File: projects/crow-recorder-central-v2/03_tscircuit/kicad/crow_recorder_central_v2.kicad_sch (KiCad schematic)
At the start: 194 parts, among them J1 C381116, J10 C9900035627, J2 C3020560, J3 C9900035627, J4 C9900035627, J5 C9900035627, J6 C9900035627, J7 C9900035627, J8 C9900035627, J9 C9900035627, Q1 C15127, Q2 C20917, U1 C6938291, U10 C6035451, U2 C181312, U3 C181312, U4 C232798, U5 C82317, U6 C2909890, U7 C5224055, U8 C5224055, U9 C79924, Y1 C2762192

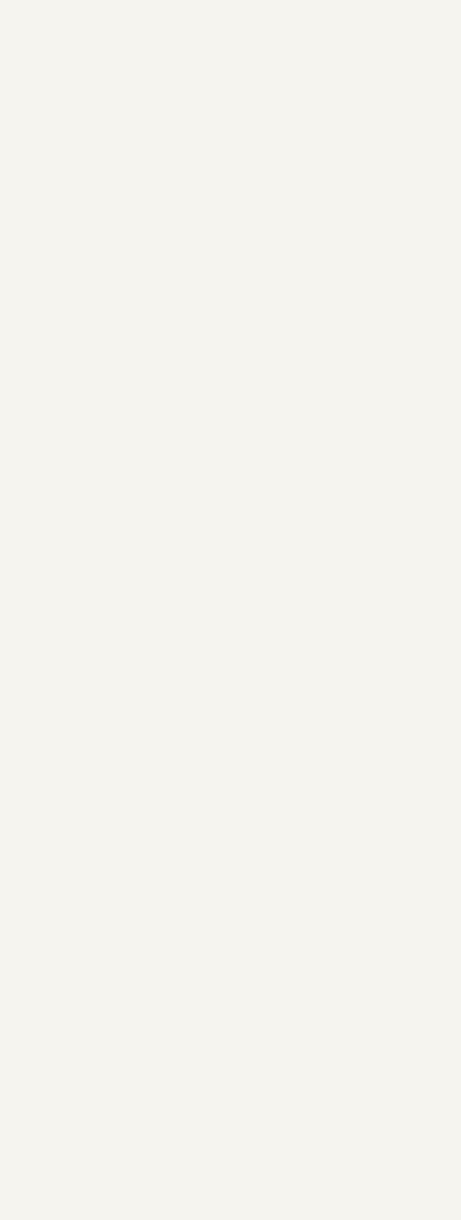
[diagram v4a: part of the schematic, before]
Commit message: crow-central v1.2: XU316 core decoupling to vendor minimum — 13x 100nF on 0V9, routing gate GREEN
Driver: 2nd external v1.1 review (EXT2-F1, archived verbatim in 08_reviews
with provenance + orchestrator verification): 8x 100nF on the 0V9 core rail
for 15 core-VDD pins vs the vendor minimum. Vendor number VERIFIED at the
source, not taken from the reviewer: XU316-1024-TQ128 ds XM-014532-PC-2.0.0
§14 'Integration' p.29 — 'Place many (at least 12) 100 nF low inductance
multi-layer ceramic capacitors close to the chip' (§H.2 p.92 agrees).

The fix (all at source, canon M3):
- tsx 8->13 C_c caps; manifest +5; promoted-sch IN-PLACE surgery (LV-strap
  precedent — regeneration drops the P5VA_4/MID2P doglegs): measured netlist
  diff vs v1.1 = EXACTLY {C_c9..C_c13} x {0V9,GND}.
- Placement: 5 anchors at scan-verified spots hard against the under-served
  pins; the 32 U1-cluster floaters PINNED at their v1.1 positions (the new
  anchors changed the legalizer walk and moved all 32 — measured — which
  would have invalidated the whole promoted chain).
- C_b0v9 slot swap: U1 courtyard vs the C_c1/C_b0v9 row leaves no 0402 slot
  at pins 50/54; the 10uF bulk (no pin-adjacency requirement, ds §14) moved
  3.75mm south; C_c11/C_c13 take its slot at 2.01/2.02mm from pins 50/54.
- Chain surgery: TDI F.Cu run -> In3 (frees the south band); 0V9 feeder
  rerouted at 0.4; 4x 0.30mm taps into pads 14/50/54/95 with scoped floors
  (0.4 into a 0.4mm-pitch row violates neighbor clearance by construction);
  C_b0v9 B.Cu feed with 2 vias; title caption relocated.
- C_c11 pad2 starved_thermal -> pad_overrides FULL (golden rule 9).

Gate: rebuild_reuse.sh from committed source = DRC 0/0/0 (severity-all +
refill + schematic-parity); port nets 115/115 + 8/8. Survival measured:
USB pair 23.621/23.511mm skew 0.110mm all-0.125 F.Cu 0 vias; U1 EP 16x
0.3/0.15 GND vias; LV straps 40/43/52 unconnected. Worst pin-to-nearest-cap
3.22mm. Per-pin map in journal/routing.md.

Co-Authored-By: Claude Opus 5 <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
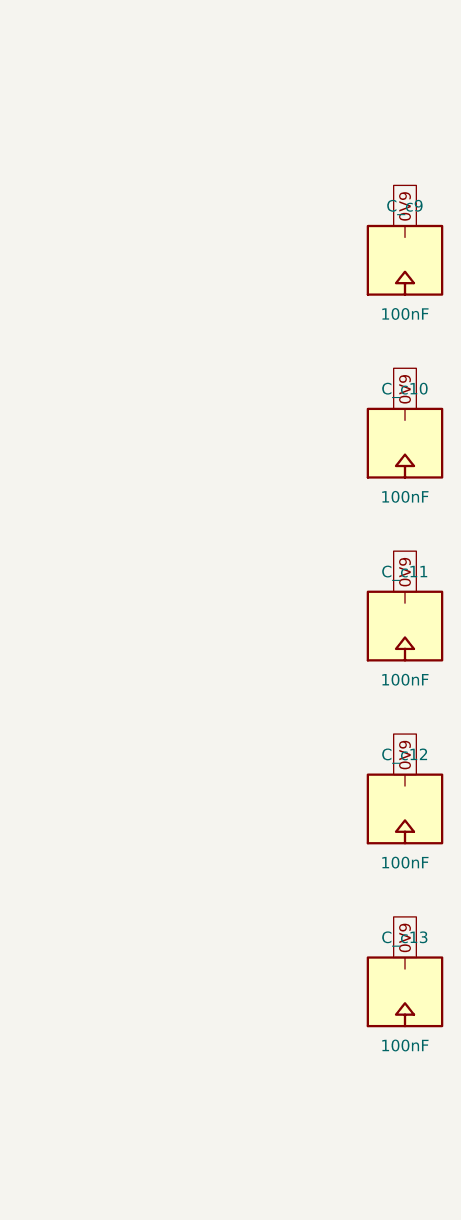
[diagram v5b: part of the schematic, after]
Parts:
- added C_c10, C_c11, C_c12, C_c13, C_c9: 100nF, Capacitor_SMD:C_0402_1005Metric, symbol elt:SYM_C_c8
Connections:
- net 0V9: now also C_c10.1, C_c11.1, C_c12.1, C_c13.1, C_c9.1
- net GND: now also C_c10.2, C_c11.2, C_c12.2, C_c13.2, C_c9.2
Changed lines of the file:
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@@
     (instances (project "crow_recorder_central_v2" (path "/735d9c2a-b8fe-44e1-a7cf-81ca2fca9464" (reference "R_inj2") (unit 1))))
+  )
+  (symbol (lib_id "elt:SYM_C_c8") (at 609.600 80.010 0) (unit 1) (in_bom yes) (on_board yes) (dnp no)
+    (property "Reference" "C_c9" (at 609.600 74.000 0) (effects (font (size 1.27 1.27))))
+    (property "Value" "100nF" (at 609.600 86.020 0) (effects (font (size 1.27 1.27))))
+    (property "Footprint" "Capacitor_SMD:C_0402_1005Metric" (at 609.600 80.010 0) (effects (font (size 1.27 1.27)) hide))
+    (pin "1")
+    (pin "2")
+    (instances (project "crow_recorder_central_v2" (path "/735d9c2a-b8fe-44e1-a7cf-81ca2fca9464" (reference "C_c9") (unit 1))))
+  )
+  (global_label "0V9" (shape passive) (at 609.600 76.200 90) (fields_autoplaced) (effects (font (size 1.27 1.27)) (justify left)))
+  (symbol (lib_id "elt:GND") (at 609.600 83.820 180) (unit 1) (in_bom no) (on_board yes) (dnp no)
+    (property "Reference" "#PWR145" (at 609.600 83.820 0) (effects (font (size 1.27 1.27)) hide))
+    (property "Value" "GND" (at 609.600 83.820 0) (effects (font (size 1.27 1.27)) hide))
+    (property "Footprint" "" (at 609.600 83.820 0) (effects (font (size 1.27 1.27)) hide))
+    (pin "1")
+    (instances (project "crow_recorder_central_v2" (path "/735d9c2a-b8fe-44e1-a7cf-81ca2fca9464" (reference "#PWR145") (unit 1))))
+  )
+  (symbol (lib_id "elt:SYM_C_c8") (at 609.600 100.330 0) (unit 1) (in_bom yes) (on_board yes) (dnp no)
+    (property "Reference" "C_c10" (at 609.600 94.320 0) (effects (font (size 1.27 1.27))))
+    (property "Value" "100nF" (at 609.600 106.340 0) (effects (font (size 1.27 1.27))))
+    (property "Footprint" "Capacitor_SMD:C_0402_1005Metric" (at 609.600 100.330 0) (effects (font (size 1.27 1.27)) hide))
+    (pin "1")
+    (pin "2")
+    (instances (project "crow_recorder_central_v2" (path "/735d9c2a-b8fe-44e1-a7cf-81ca2fca9464" (reference "C_c10") (unit 1))))
+  )
+  (global_label "0V9" (shape passive) (at 609.600 96.520 90) (fields_autoplaced) (effects (font (size 1.27 1.27)) (justify left)))
+  (symbol (lib_id "elt:GND") (at 609.600 104.140 180) (unit 1) (in_bom no) (on_board yes) (dnp no)
+    (property "Reference" "#PWR146" (at 609.600 104.140 0) (effects (font (size 1.27 1.27)) hide))
+    (property "Value" "GND" (at 609.600 104.140 0) (effects (font (size 1.27 1.27)) hide))
+    (property "Footprint" "" (at 609.600 104.140 0) (effects (font (size 1.27 1.27)) hide))
+    (pin "1")
+    (instances (project "crow_recorder_central_v2" (path "/735d9c2a-b8fe-44e1-a7cf-81ca2fca9464" (reference "#PWR146") (unit 1))))
+  )
+  (symbol (lib_id "elt:SYM_C_c8") (at 609.600 120.650 0) (unit 1) (in_bom yes) (on_board yes) (dnp no)
+    (property "Reference" "C_c11" (at 609.600 114.640 0) (effects (font (size 1.27 1.27))))
+    (property "Value" "100nF" (at 609.600 126.660 0) (effects (font (size 1.27 1.27))))
+    (property "Footprint" "Capacitor_SMD:C_0402_1005Metric" (at 609.600 120.650 0) (effects (font (size 1.27 1.27)) hide))
+    (pin "1")
+    (pin "2")
+    (instances (project "crow_recorder_central_v2" (path "/735d9c2a-b8fe-44e1-a7cf-81ca2fca9464" (reference "C_c11") (unit 1))))
+  )
+  (global_label "0V9" (shape passive) (at 609.600 116.840 90) (fields_autoplaced) (effects (font (size 1.27 1.27)) (justify left)))
+  (symbol (lib_id "elt:GND") (at 609.600 124.460 180) (unit 1) (in_bom no) (on_board yes) (dnp no)
+    (property "Reference" "#PWR147" (at 609.600 124.460 0) (effects (font (size 1.27 1.27)) hide))
+    (property "Value" "GND" (at 609.600 124.460 0) (effects (font (size 1.27 1.27)) hide))
+    (property "Footprint" "" (at 609.600 124.460 0) (effects (font (size 1.27 1.27)) hide))
+    (pin "1")
+    (instances (project "crow_recorder_central_v2" (path "/735d9c2a-b8fe-44e1-a7cf-81ca2fca9464" (reference "#PWR147") (unit 1))))
+  )
+  (symbol (lib_id "elt:SYM_C_c8") (at 609.600 140.970 0) (unit 1) (in_bom yes) (on_board yes) (dnp no)
+    (property "Reference" "C_c12" (at 609.600 134.960 0) (effects (font (size 1.27 1.27))))
+    (property "Value" "100nF" (at 609.600 146.980 0) (effects (font (size 1.27 1.27))))
+    (property "Footprint" "Capacitor_SMD:C_0402_1005Metric" (at 609.600 140.970 0) (effects (font (size 1.27 1.27)) hide))
+    (pin "1")
+    (pin "2")
+    (instances (project "crow_recorder_central_v2" (path "/735d9c2a-b8fe-44e1-a7cf-81ca2fca9464" (reference "C_c12") (unit 1))))
+  )
+  (global_label "0V9" (shape passive) (at 609.600 137.160 90) (fields_autoplaced) (effects (font (size 1.27 1.27)) (justify left)))
+  (symbol (lib_id "elt:GND") (at 609.600 144.780 180) (unit 1) (in_bom no) (on_board yes) (dnp no)
+    (property "Reference" "#PWR148" (at 609.600 144.780 0) (effects (font (size 1.27 1.27)) hide))
+    (property "Value" "GND" (at 609.600 144.780 0) (effects (font (size 1.27 1.27)) hide))
+    (property "Footprint" "" (at 609.600 144.780 0) (effects (font (size 1.27 1.27)) hide))
+    (pin "1")
+    (instances (project "crow_recorder_central_v2" (path "/735d9c2a-b8fe-44e1-a7cf-81ca2fca9464" (reference "#PWR148") (unit 1))))
+  )
+  (symbol (lib_id "elt:SYM_C_c8") (at 609.600 161.290 0) (unit 1) (in_bom yes) (on_board yes) (dnp no)
+    (property "Reference" "C_c13" (at 609.600 155.280 0) (effects (font (size 1.27 1.27))))
+    (property "Value" "100nF" (at 609.600 167.300 0) (effects (font (size 1.27 1.27))))
+    (property "Footprint" "Capacitor_SMD:C_0402_1005Metric" (at 609.600 161.290 0) (effects (font (size 1.27 1.27)) hide))
+    (pin "1")
+    (pin "2")
+    (instances (project "crow_recorder_central_v2" (path "/735d9c2a-b8fe-44e1-a7cf-81ca2fca9464" (reference "C_c13") (unit 1))))
+  )
+  (global_label "0V9" (shape passive) (at 609.600 157.480 90) (fields_autoplaced) (effects (font (size 1.27 1.27)) (justify left)))
+  (symbol (lib_id "elt:GND") (at 609.600 165.100 180) (unit 1) (in_bom no) (on_board yes) (dnp no)
+    (property "Reference" "#PWR149" (at 609.600 165.100 0) (effects (font (size 1.27 1.27)) hide))
+    (property "Value" "GND" (at 609.600 165.100 0) (effects (font (size 1.27 1.27)) hide))
+    (property "Footprint" "" (at 609.600 165.100 0) (effects (font (size 1.27 1.27)) hide))
+    (pin "1")
+    (instances (project "crow_recorder_central_v2" (path "/735d9c2a-b8fe-44e1-a7cf-81ca2fca9464" (reference "#PWR149") (unit 1))))
   )
   (sheet_instances (path "/" (page "1")))
